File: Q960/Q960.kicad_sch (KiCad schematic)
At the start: 13 parts, among them J101 BAT(3V), J102 BAT(4.5V), SW101 TS-06104, U1 LP2950-3.3_TO92, U101 SeeeduinoXIAO, U102 S-2110A, U103 S-2110A

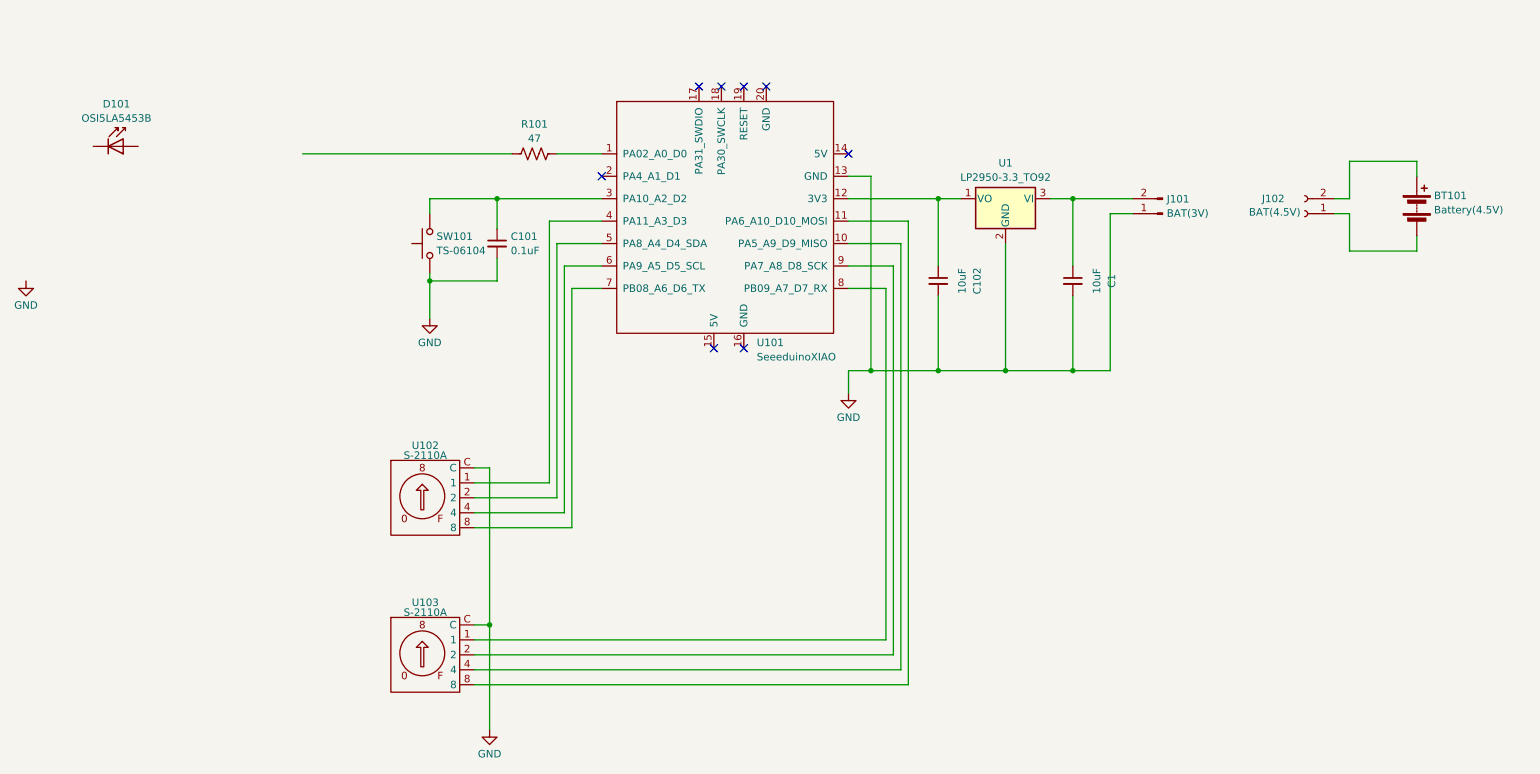
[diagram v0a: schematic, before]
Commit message: LED駆動回路追加:基板なし
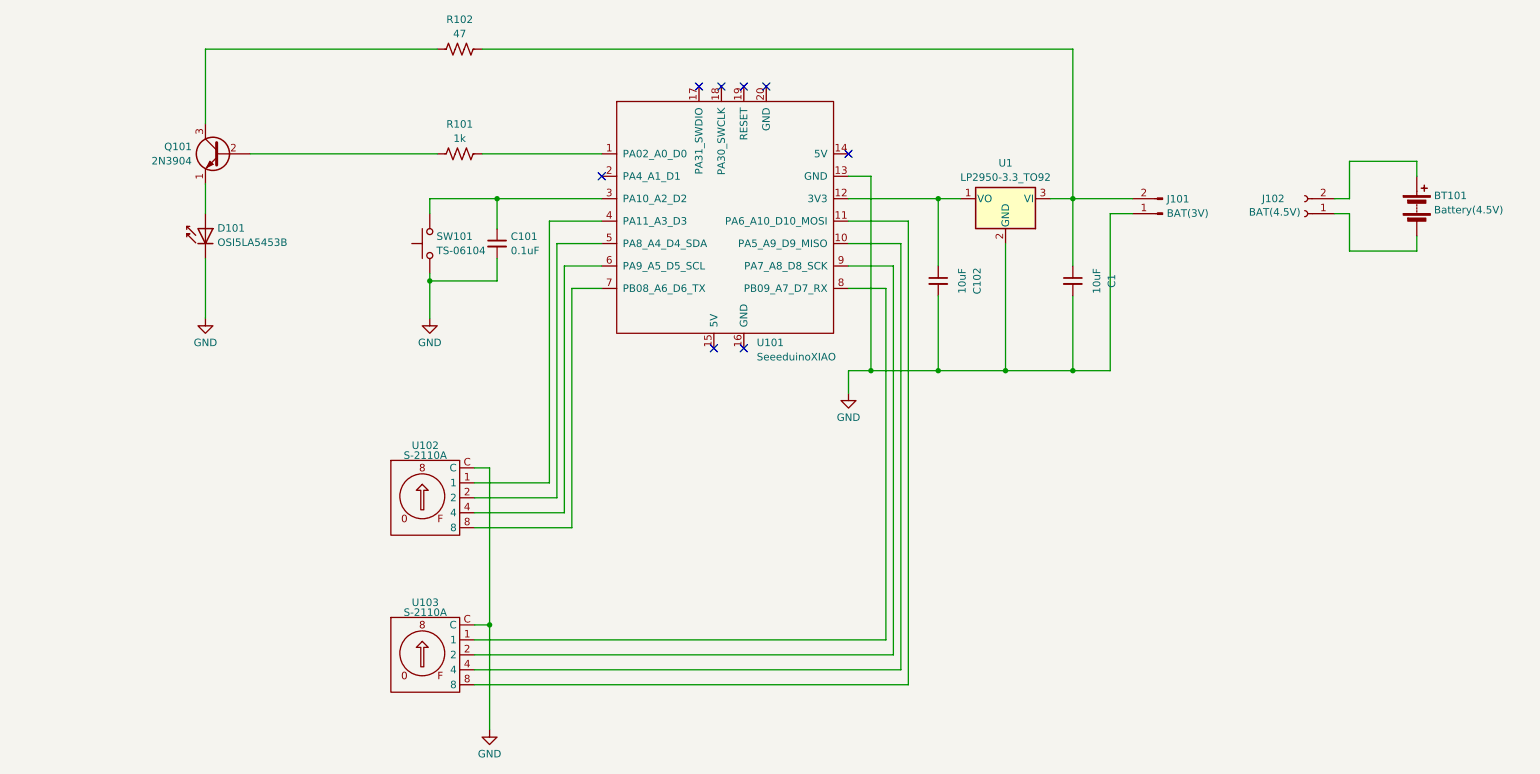
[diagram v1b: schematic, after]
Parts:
- added Q101: 2N3904, Package_TO_SOT_THT:TO-92_Inline, symbol Transistor_BJT:2N3904
- added R102: 47, Resistor_SMD:R_0603_1608Metric_Pad0.98x0.95mm_HandSolder, symbol Device:R_US
- R101: value 47 -> 1k
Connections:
- net GND: now also D101.1 (K)
- net at C1.1, J101.2 (Pin_2), U1.3 (VI): now also R102.2
- net at R101.1: now also Q101.2 (B)
- net at D101.2 (A): now also Q101.1 (E)
- new net: Q101.3 (C), R102.1
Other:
- moved on the sheet: D101, R101
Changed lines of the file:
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@@
+	(wire
+		(pts
+			(xy 60.96 26.67) (xy 60.96 39.37)
+		)
+		(stroke
+			(width 0)
+			(type default)
+		)
+	)
 	(wire
 		(pts
@@
 	(wire
 		(pts
+			(xy 60.96 54.61) (xy 60.96 49.53)
+		)
+		(stroke
+			(width 0)
+			(type default)
+		)
+	)
+	(wire
+		(pts
 			(xy 196.85 81.28) (xy 208.28 81.28)
 		)
@@
 	(wire
 		(pts
+			(xy 60.96 72.39) (xy 60.96 62.23)
+		)
+		(stroke
+			(width 0)
+			(type default)
+		)
+	)
+	(wire
+		(pts
 			(xy 255.27 54.61) (xy 255.27 60.96)
 		)
@@
 	(wire
 		(pts
+			(xy 208.28 26.67) (xy 107.95 26.67)
+		)
+		(stroke
+			(width 0)
+			(type default)
+		)
+	)
+	(wire
+		(pts
 			(xy 106.68 97.79) (xy 109.22 97.79)
 		)
@@
 	(wire
 		(pts
-			(xy 120.65 44.45) (xy 128.27 44.45)
+			(xy 107.95 44.45) (xy 128.27 44.45)
 		)
 		(stroke
@@
 	(wire
 		(pts
-			(xy 77.47 44.45) (xy 113.03 44.45)
+			(xy 68.58 44.45) (xy 100.33 44.45)
 		)
 		(stroke
@@
 		(pts
 			(xy 208.28 81.28) (xy 214.63 81.28)
+		)
+		(stroke
+			(width 0)
+			(type default)
+		)
+	)
+	(wire
+		(pts
+			(xy 208.28 52.07) (xy 208.28 26.67)
+		)
+		(stroke
+			(width 0)
+			(type default)
+		)
+	)
+	(wire
+		(pts
+			(xy 100.33 26.67) (xy 60.96 26.67)
 		)
 		(stroke
@@
 	)
 	(symbol
+		(lib_id "Transistor_BJT:2N3904")
+		(at 63.5 44.45 0)
+		(mirror y)
+		(unit 1)
+		(exclude_from_sim no)
+		(in_bom yes)
+		(on_board yes)
+		(dnp no)
+		(fields_autoplaced yes)
+		(property "Reference" "Q101"
+			(at 58.6486 43.2378 0)
+			(effects
+				(font
+					(size 1.27 1.27)
+				)
+				(justify left)
+			)
+		)
+		(property "Value" "2N3904"
+			(at 58.6486 45.6621 0)
+			(effects
+				(font
+					(size 1.27 1.27)
+				)
+				(justify left)
+			)
+		)
+		(property "Footprint" "Package_TO_SOT_THT:TO-92_Inline"
+			(at 58.42 46.355 0)
+			(effects
+				(font
+					(size 1.27 1.27)
+					(italic yes)
+				)
+				(justify left)
+				(hide yes)
+			)
+		)
+		(property "Datasheet" "https://www.onsemi.com/pub/Collateral/2N3903-D.PDF"
+			(at 63.5 44.45 0)
+			(effects
+				(font
+					(size 1.27 1.27)
+				)
+				(justify left)
+				(hide yes)
+			)
+		)
+		(property "Description" "0.2A Ic, 40V Vce, Small Signal NPN Transistor, TO-92"
+			(at 63.5 44.45 0)
+			(effects
+				(font
+					(size 1.27 1.27)
+				)
+				(hide yes)
+			)
+		)
+		(pin "1"
+		)
+		(pin "2"
+		)
+		(pin "3"
+		)
+		(instances
+			(project ""
+				(path "/aa9b1917-073a-48a7-b08f-90b406395592"
+					(reference "Q101")
+					(unit 1)
+				)
+			)
+		)
+	)
+	(symbol
 		(lib_id "power:GND")
 		(at 109.22 142.24 0)
@@
 	(symbol
 		(lib_id "power:GND")
-		(at 30.48 66.04 0)
+		(at 60.96 72.39 0)
 		(unit 1)
 		(exclude_from_sim no)
@@
 		(fields_autoplaced yes)
 		(property "Reference" "#PWR0103"
-			(at 30.48 72.39 0)
+			(at 60.96 78.74 0)
 			(effects
 				(font
@@
 		)
 		(property "Value" "GND"
-			(at 30.48 70.1731 0)
+			(at 60.96 76.5231 0)
 			(effects
 				(font
@@
 		)
 		(property "Footprint" ""
-			(at 30.48 66.04 0)
+			(at 60.96 72.39 0)
 			(effects
 				(font
@@
 		)
 		(property "Datasheet" ""
-			(at 30.48 66.04 0)
+			(at 60.96 72.39 0)
 			(effects
 				(font
@@
 		)
 		(property "Description" "Power symbol creates a global label with name \"GND\" , ground"
-			(at 30.48 66.04 0)
+			(at 60.96 72.39 0)
 			(effects
 				(font
@@
 	(symbol
 		(lib_id "Device:R_US")
-		(at 116.84 44.45 90)
+		(at 104.14 44.45 90)
 		(unit 1)
 		(exclude_from_sim no)
@@
 		(fields_autoplaced yes)
 		(property "Reference" "R101"
-			(at 116.84 39.4165 90)
-			(effects
-				(font
-					(size 1.27 1.27)
-				)
-			)
-		)
-		(property "Value" "47"
-			(at 116.84 41.8408 90)
+			(at 104.14 39.4165 90)
+			(effects
+				(font
+					(size 1.27 1.27)
+				)
+			)
+		)
+		(property "Value" "1k"
+			(at 104.14 41.8408 90)
 			(effects
 				(font
@@
 		)
 		(property "Footprint" "Resistor_SMD:R_0603_1608Metric_Pad0.98x0.95mm_HandSolder"
-			(at 117.094 43.434 90)
+			(at 104.394 43.434 90)
 			(effects
 				(font
@@
 		)
 		(property "Datasheet" "~"
-			(at 116.84 44.45 0)
+			(at 104.14 44.45 0)
 			(effects
 				(font
@@
 		)
 		(property "Description" "Resistor, US symbol"
-			(at 116.84 44.45 0)
+			(at 104.14 44.45 0)
 			(effects
 				(font
@@
 	)
 	(symbol
+		(lib_id "Device:R_US")
+		(at 104.14 26.67 90)
+		(unit 1)
+		(exclude_from_sim no)
+		(in_bom yes)
+		(on_board yes)
+		(dnp no)
+		(fields_autoplaced yes)
+		(property "Reference" "R102"
+			(at 104.14 21.6365 90)
+			(effects
+				(font
+					(size 1.27 1.27)
+				)
+			)
+		)
+		(property "Value" "47"
+			(at 104.14 24.0608 90)
+			(effects
+				(font
+					(size 1.27 1.27)
+				)
+			)
+		)
+		(property "Footprint" "Resistor_SMD:R_0603_1608Metric_Pad0.98x0.95mm_HandSolder"
+			(at 104.394 25.654 90)
+			(effects
+				(font
+					(size 1.27 1.27)
+				)
+				(hide yes)
+			)
+		)
+		(property "Datasheet" "~"
+			(at 104.14 26.67 0)
+			(effects
+				(font
+					(size 1.27 1.27)
+				)
+				(hide yes)
+			)
+		)
+		(property "Description" "Resistor, US symbol"
+			(at 104.14 26.67 0)
+			(effects
+				(font
+					(size 1.27 1.27)
+				)
+				(hide yes)
+			)
+		)
+		(pin "1"
+		)
+		(pin "2"
+		)
+		(instances
+			(project "Q960"
+				(path "/aa9b1917-073a-48a7-b08f-90b406395592"
+					(reference "R102")
+					(unit 1)
+				)
+			)
+		)
+	)
+	(symbol
 		(lib_id "Device:C_Small")
 		(at 208.28 66.04 0)
@@
 	(symbol
 		(lib_id "LED:LD271")
-		(at 46.99 43.18 0)
+		(at 60.96 57.15 90)
 		(unit 1)
 		(exclude_from_sim no)
@@
 		(fields_autoplaced yes)
 		(property "Reference" "D101"
-			(at 45.847 35.9875 0)
-			(effects
-				(font
-					(size 1.27 1.27)
-				)
+			(at 62.992 57.0808 90)
+			(effects
+				(font
+					(size 1.27 1.27)
+				)
+				(justify right)
 			)
 		)
 		(property "Value" "OSI5LA5453B"
-			(at 45.847 38.4118 0)
-			(effects
-				(font
-					(size 1.27 1.27)
-				)
+			(at 62.992 59.5051 90)
+			(effects
+				(font
+					(size 1.27 1.27)
+				)
+				(justify right)
 			)
 		)
 		(property "Footprint" "LED_THT:LED_D5.0mm_IRGrey"
-			(at 46.99 38.735 0)
+			(at 56.515 57.15 0)
 			(effects
 				(font
@@
 		)
 		(property "Datasheet" "http://www.alliedelec.com/m/d/40788c34903a719969df15f1fbea1056.pdf"
-			(at 45.72 43.18 0)
+			(at 60.96 58.42 0)
 			(effects
 				(font
@@
 		)
 		(property "Description" "940nm IR-LED, 5mm"
-			(at 46.99 43.18 0)
-			(effects
-				(font
+			(at 60.96 57.15 0)
+			(effects
+				(font
